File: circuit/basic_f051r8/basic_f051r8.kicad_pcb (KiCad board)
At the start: 2 copper layers, 118.4 x 65.2 mm, 61 parts, among them J1 Conn_01x04_Male, J2 Conn_01x03_Male, J3 USB_B, J4 Conn_01x02_Male, J5 Conn_01x02_Male, J6 Conn_01x02_Male, J7 Conn_01x02_Male, Q1 2N3904, Q2 IRF540N, Q3 IRF540N, Q4 IRF540N, Q5 IRF540N, SW1 SW_Push, SW2 SW_Push, U1 STM32F051R8Tx, U2 AMS1117-5.0, U3 H11L1, U4 FT232RL, U5 4N35, U6 4N35, U7 4N35, U8 4N35

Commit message: PCB 3D components
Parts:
- moved J3 4.11 mm to (191.3, 84.4)
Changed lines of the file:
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@@
     (pad "3" thru_hole oval (at 10 0 90) (size 1.98 3.96) (drill 1.32) (layers *.Cu *.Mask)
       (net 2 "GND") (pinfunction "Pin_3") (pintype "passive"))
-    (model "${KICAD6_3DMODEL_DIR}/TerminalBlock.3dshapes/TerminalBlock_Altech_AK300-3_P5.00mm.wrl"
-      (offset (xyz 0 0 0))
-      (scale (xyz 1 1 1))
-      (rotate (xyz 0 0 0))
+    (model "${KIPRJMOD}/libs/pkg3d/BR1103V.stp"
+      (offset (xyz -12 -4 0))
+      (scale (xyz 0.5 0.5 0.5))
+      (rotate (xyz -90 0 0))
     )
   )
@@
     (pad "2" thru_hole oval (at 5 0) (size 1.98 3.96) (drill 1.32) (layers *.Cu *.Mask)
       (net 23 "PORT_INJB") (pinfunction "Pin_2") (pintype "passive"))
-    (model "${KICAD6_3DMODEL_DIR}/TerminalBlock.3dshapes/TerminalBlock_Altech_AK300-2_P5.00mm.wrl"
-      (offset (xyz 0 0 0))
-      (scale (xyz 1 1 1))
-      (rotate (xyz 0 0 0))
+    (model "${KIPRJMOD}/libs/pkg3d/BR1102V.stp"
+      (offset (xyz -2 -4 0))
+      (scale (xyz 0.5 0.5 0.5))
+      (rotate (xyz -90 0 0))
     )
   )
@@
   )
   (footprint "Connector_USB:USB_B_Lumberg_2411_02_Horizontal" (layer "F.Cu")
-    (at 191.54 88.4975 90)
+    (at 191.35 84.3875 90)
     (descr "USB 2.0 receptacle type B, horizontal version, through-hole, https://downloads.lumberg.com/datenblaetter/en/2411_02.pdf")
     (tags "USB B receptacle horizontal through-hole")
@@
     (pad "5" thru_hole circle (at 4.86 -4.75 180) (size 4 4) (drill 2.3) (layers *.Cu *.Mask)
       (net 2 "GND") (pinfunction "Shield") (pintype "passive"))
-    (model "${KICAD6_3DMODEL_DIR}/Connector_USB.3dshapes/USB_B_Lumberg_2411_02_Horizontal.wrl"
-      (offset (xyz 0 0 0))
-      (scale (xyz 1 1 1))
-      (rotate (xyz 0 0 0))
+    (model "${KIPRJMOD}/libs/pkg3d/usb-b.stp"
+      (offset (xyz -2 -7.5 0))
+      (scale (xyz 1 1 1))
+      (rotate (xyz -90 0 -90))
     )
   )
@@
     (pad "2" thru_hole oval (at 5 0 90) (size 1.98 3.96) (drill 1.32) (layers *.Cu *.Mask)
       (net 4 "GNDPWR") (pinfunction "Pin_2") (pintype "passive"))
-    (model "${KICAD6_3DMODEL_DIR}/TerminalBlock.3dshapes/TerminalBlock_Altech_AK300-2_P5.00mm.wrl"
-      (offset (xyz 0 0 0))
-      (scale (xyz 1 1 1))
-      (rotate (xyz 0 0 0))
+    (model "${KIPRJMOD}/libs/pkg3d/BR1102V.stp"
+      (offset (xyz -2 -4 0))
+      (scale (xyz 0.5 0.5 0.5))
+      (rotate (xyz -90 0 0))
     )
   )
@@
     (pad "2" thru_hole oval (at 5 0 90) (size 1.98 3.96) (drill 1.32) (layers *.Cu *.Mask)
       (net 2 "GND") (pinfunction "Pin_2") (pintype "passive"))
-    (model "${KICAD6_3DMODEL_DIR}/TerminalBlock.3dshapes/TerminalBlock_Altech_AK300-2_P5.00mm.wrl"
-      (offset (xyz 0 0 0))
-      (scale (xyz 1 1 1))
-      (rotate (xyz 0 0 0))
+    (model "${KIPRJMOD}/libs/pkg3d/BR1102V.stp"
+      (offset (xyz -2 -4 0))
+      (scale (xyz 0.5 0.5 0.5))
+      (rotate (xyz -90 0 0))
     )
   )
@@
     (pad "2" thru_hole oval (at 5 0) (size 1.98 3.96) (drill 1.32) (layers *.Cu *.Mask)
       (net 20 "PORT_IGNB") (pinfunction "Pin_2") (pintype "passive"))
-    (model "${KICAD6_3DMODEL_DIR}/TerminalBlock.3dshapes/TerminalBlock_Altech_AK300-2_P5.00mm.wrl"
-      (offset (xyz 0 0 0))
-      (scale (xyz 1 1 1))
-      (rotate (xyz 0 0 0))
-    )
-  )
+    (model "${KIPRJMOD}/libs/pkg3d/BR1102V.stp"
+      (offset (xyz -2 -4 0))
+      (scale (xyz 0.5 0.5 0.5))
+      (rotate (xyz -90 0 0))
+    )
+  )

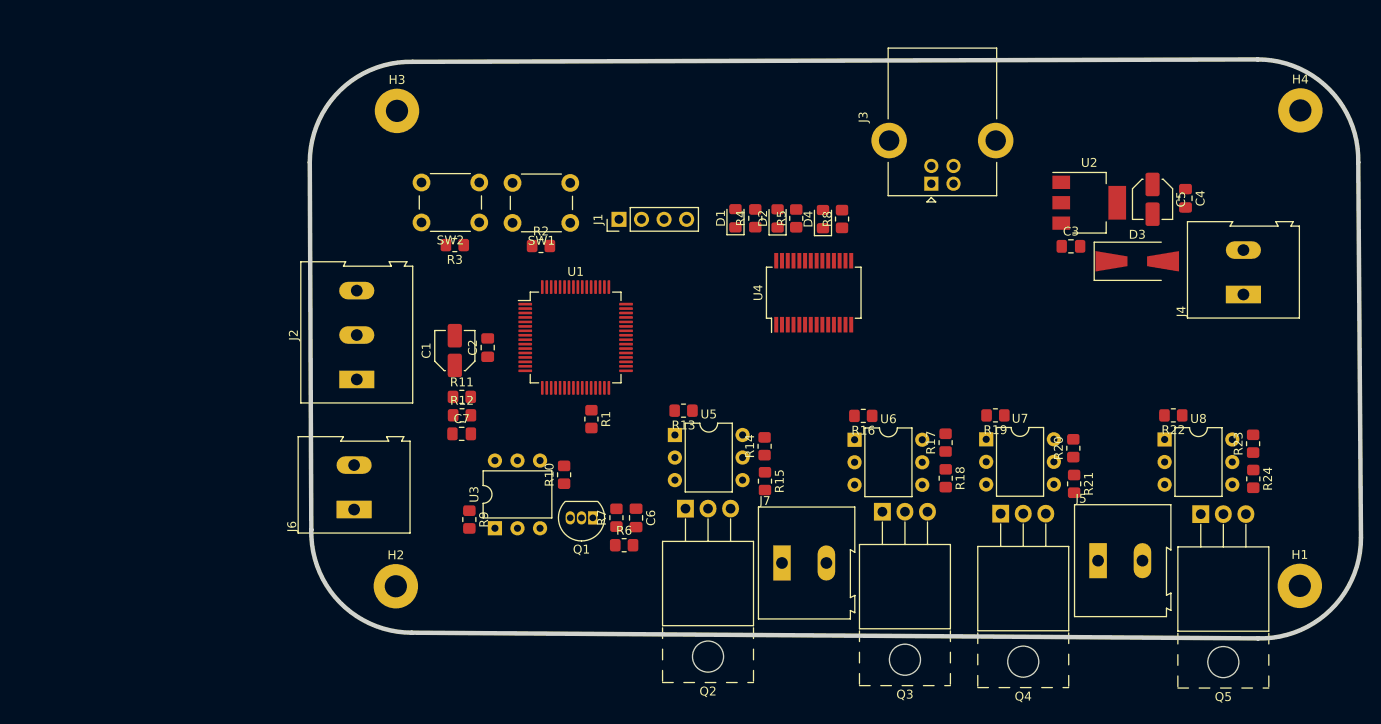
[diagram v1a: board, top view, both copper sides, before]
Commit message: PCB Draft Done
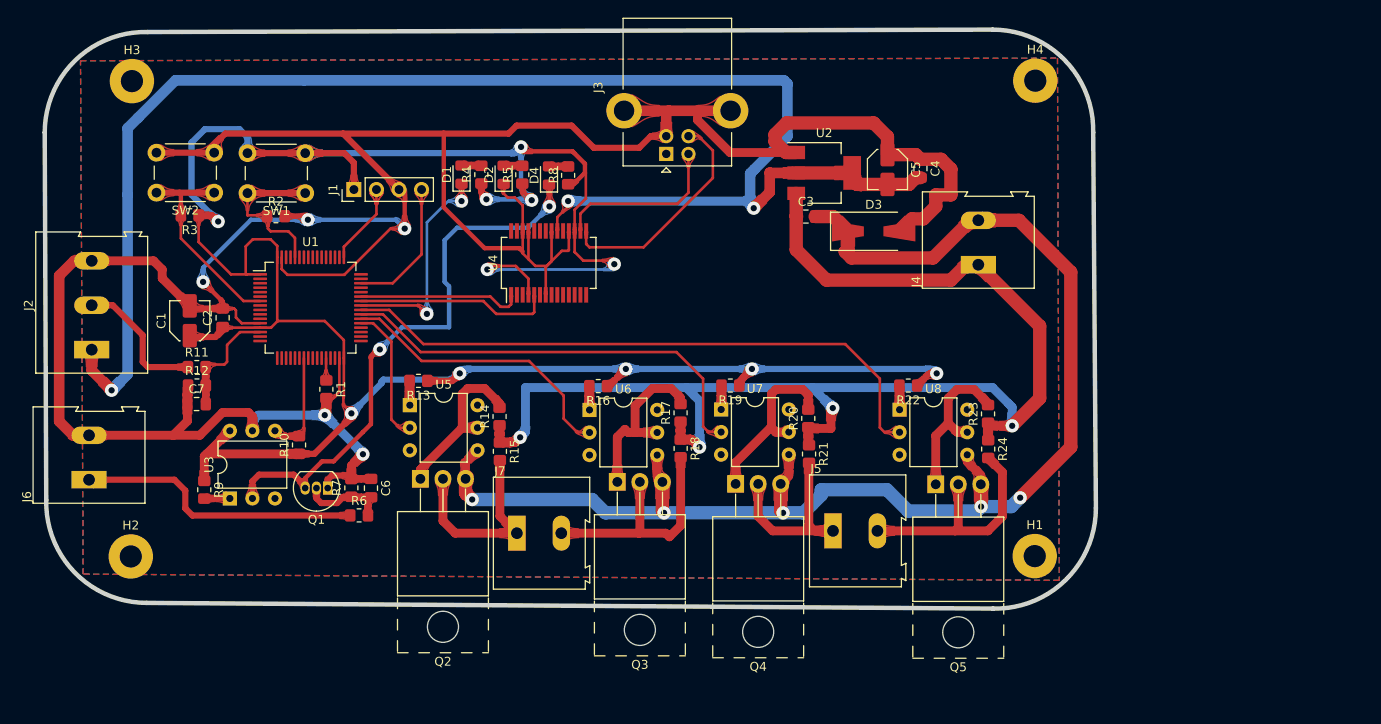
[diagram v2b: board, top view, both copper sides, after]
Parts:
- moved D1 31.2 mm to (138.5, 83.4)
- moved D2 31.2 mm to (143.2, 83.4)
- moved D4 31.2 mm to (148.3, 83.5)
- moved R4 31.2 mm to (140.7, 83.4)
- moved R5 31.2 mm to (145.3, 83.4)
- moved R8 31.2 mm to (150.5, 83.4)
- moved U4 30.0 mm to (148.3, 93.3)
- moved J1 30.0 mm to (126.3, 85.0)
- moved Q1 30.0 mm to (123.4, 118.7)
- moved R1 30.0 mm to (123.2, 107.5)
- moved R11 30.0 mm to (108.6, 105.0)
- moved R7 30.0 mm to (126.0, 118.6)
- moved R9 30.0 mm to (109.5, 118.8)
- moved U1 30.0 mm to (121.5, 98.3)
- moved C2 30.0 mm to (111.6, 99.5)
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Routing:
- net GND: track 0.00 -> 348.5 mm, vias 0 -> 5
- net VDD: track 0.00 -> 287.0 mm, vias 0 -> 11
- net VCC: track 0.00 -> 176.5 mm, vias 0 -> 3
- net GNDPWR: track 0.00 -> 156.5 mm, vias 0 -> 5
- net +12V: track 0.00 -> 146.4 mm, vias 0 -> 4
- net OUT_IGNB: track 0.00 -> 69.6 mm
- net Net-(D4-Pad1): track 0.00 -> 63.6 mm, vias 0 -> 2
- net OUT_IGNA: track 0.00 -> 49.2 mm
- net OUT_INJB: track 0.00 -> 32.6 mm
- net CRANK_PORT: track 0.00 -> 32.2 mm
- net PORT_INJB: track 0.00 -> 27.6 mm
- net PORT_IGNB: track 0.00 -> 27.4 mm
- net Net-(U4-Pad15): track 0.00 -> 25.6 mm
- net LED_NOPULSE: track 0.00 -> 25.0 mm, vias 0 -> 2
- net NRST: track 0.00 -> 23.6 mm
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- added copper zone on B.Cu, net (none)
- added copper zone on F.Cu, net (none)
